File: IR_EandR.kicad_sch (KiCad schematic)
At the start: 4 parts, among them J4 IR Emitter, J6 Conn_01x04

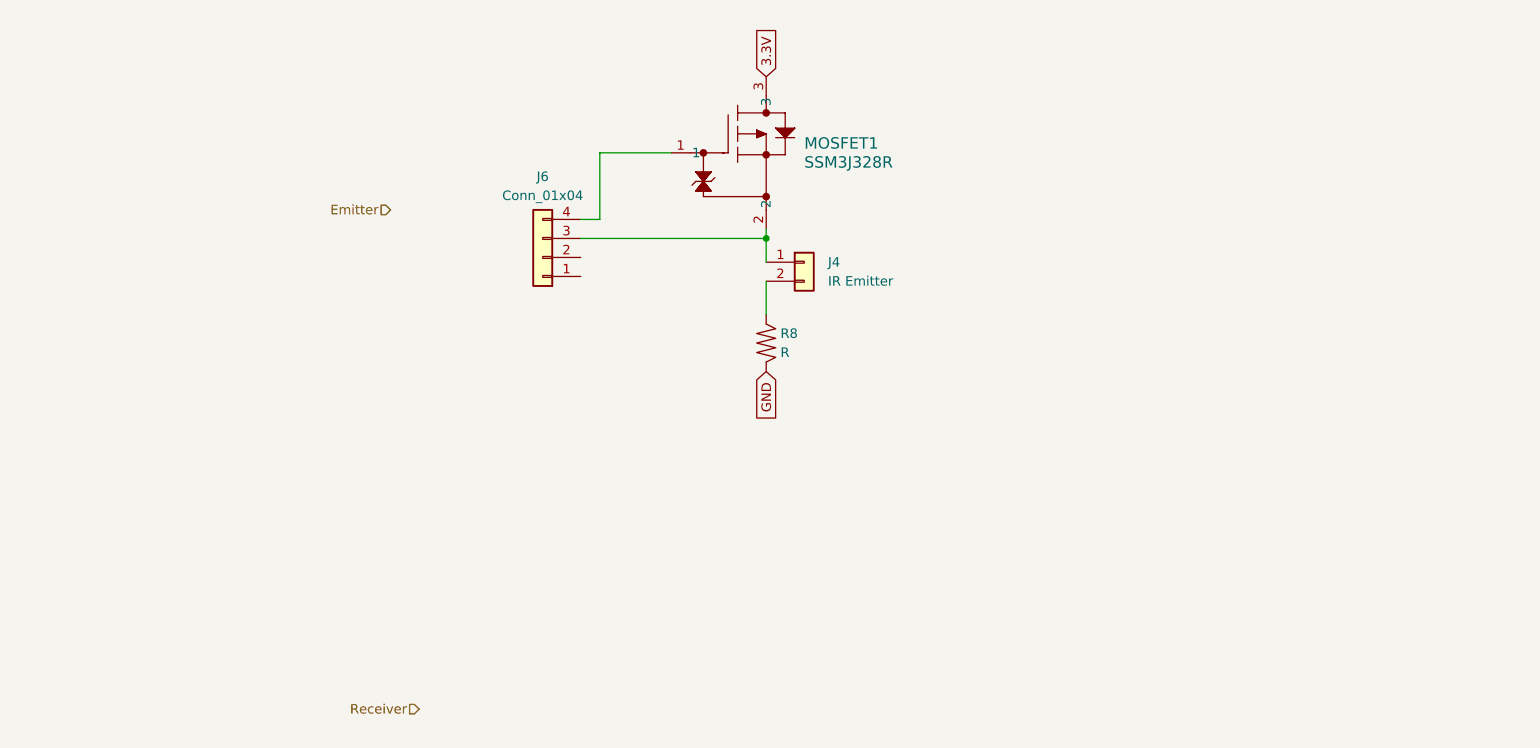
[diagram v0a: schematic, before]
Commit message: IR Receiver and Comparator
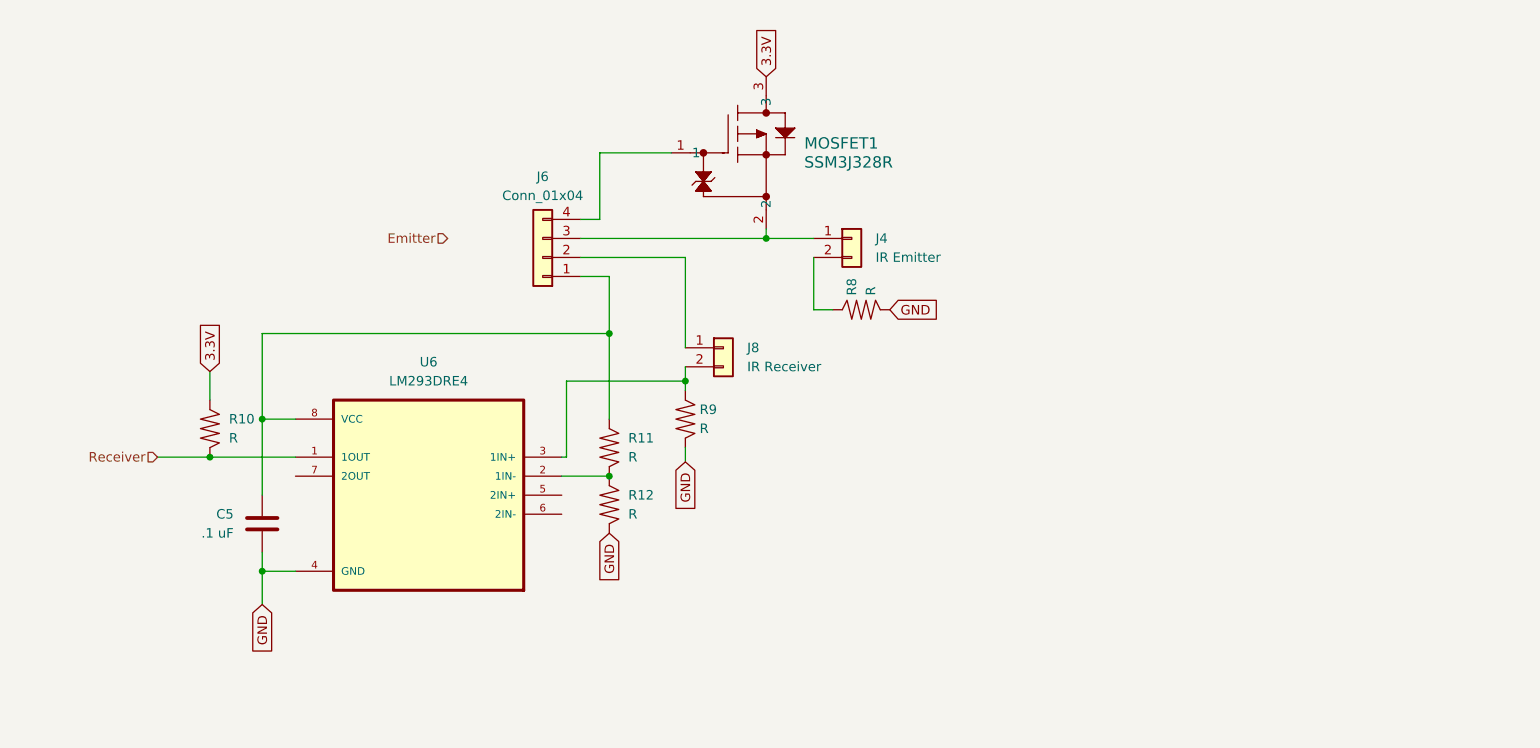
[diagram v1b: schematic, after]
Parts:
- added C5: .1 uF, symbol Hestres_Standard_Lib:C
- added J8: IR Receiver, symbol Connector_Generic:Conn_01x02
- added R10, R11, R12, R9: R, symbol Hestres_Standard_Lib:R
- added U6: LM293DRE4, LM293DRE4:SOIC127P599X175-8N, symbol ProjComparator:LM293DRE4
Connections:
- net 3.3V: now also R10.1
- net GND: now also C5.2, R12.2, R9.2, U6.4 (GND)
- net Receiver: now also R10.2, U6.1 (1OUT)
- net at J6.1 (Pin_1): now also C5.1, R11.1, U6.8 (VCC)
- net at J6.2 (Pin_2): now also J8.1 (Pin_1)
- new net: R11.2, R12.1, U6.2 (1IN-)
- new net: J8.2 (Pin_2), R9.1, U6.3 (1IN+)
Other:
- moved on the sheet: J4, R8

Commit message: Some cleanup
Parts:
- C5: footprint (none) -> Capacitor_SMD:C_0805_2012Metric
- MOSFET1: footprint SOT-23F_TOS -> (none)
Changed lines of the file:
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@@
       (effects (font (size 1.524 1.524)) (justify left))
     )
-    (property "Footprint" "SOT-23F_TOS" (at 130.175 49.53 0)
+    (property "Footprint" "" (at 130.175 49.53 0)
       (effects (font (size 1.27 1.27) italic) hide)
     )
@@
       (effects (font (size 1.27 1.27)) (justify left))
     )
-    (property "Footprint" "" (at 72.0598 110.49 0)
-      (effects (font (size 1.27 1.27)) hide)
-    )
+    (property "Footprint" "Capacitor_SMD:C_0805_2012Metric" (at 72.0598 110.49 0)
+      (effects (font (size 1.27 1.27)) hide)
+    )

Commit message: Remaining Footprints Assigned
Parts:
- J8: footprint (none) -> Connector_PinHeader_2.54mm:PinHeader_1x02_P2.54mm_Vertical
- MOSFET1: footprint (none) -> Proj:SOT-23F_TOS
- R10, R11, R12, R9: footprint (none) -> Resistor_SMD:R_0805_2012Metric
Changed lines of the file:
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@@
       (effects (font (size 1.524 1.524)) (justify left))
     )
-    (property "Footprint" "" (at 130.175 49.53 0)
+    (property "Footprint" "Proj:SOT-23F_TOS" (at 130.175 49.53 0)
       (effects (font (size 1.27 1.27) italic) hide)
     )
@@
       (effects (font (size 1.27 1.27)) (justify left))
     )
-    (property "Footprint" "" (at 117.602 96.52 90)
+    (property "Footprint" "Resistor_SMD:R_0805_2012Metric" (at 117.602 96.52 90)
       (effects (font (size 1.27 1.27)) hide)
     )
@@
       (effects (font (size 1.27 1.27)) (justify left))
     )
-    (property "Footprint" "" (at 127.762 92.71 90)
+    (property "Footprint" "Resistor_SMD:R_0805_2012Metric" (at 127.762 92.71 90)
       (effects (font (size 1.27 1.27)) hide)
     )
@@
       (effects (font (size 1.27 1.27)) (justify left))
     )
-    (property "Footprint" "" (at 64.262 93.98 90)
+    (property "Footprint" "Resistor_SMD:R_0805_2012Metric" (at 64.262 93.98 90)
       (effects (font (size 1.27 1.27)) hide)
     )
@@
       (effects (font (size 1.27 1.27)) (justify left))
     )
-    (property "Footprint" "" (at 117.602 104.14 90)
+    (property "Footprint" "Resistor_SMD:R_0805_2012Metric" (at 117.602 104.14 90)
       (effects (font (size 1.27 1.27)) hide)
     )
@@
       (effects (font (size 1.27 1.27)) (justify left))
     )
-    (property "Footprint" "" (at 134.62 83.185 0)
+    (property "Footprint" "Connector_PinHeader_2.54mm:PinHeader_1x02_P2.54mm_Vertical" (at 134.62 83.185 0)
       (effects (font (size 1.27 1.27)) hide)
     )

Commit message: Annotations
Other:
- note added: "Pins 1 and 2 of this jumper allow the comparator and IR Receiver to be driven at 3.3V or 18V."
- note added: "Pins 3 and 4 allow me to connect the IR Emitter directly to the MCU or through a FET to VCC. This will depend on how much current is needed for the distances I plan to send the IR beam. By using a through-pin IR Diode, I also leave myself open to switch to a laser emitter if needed."
- note added: "R11 and R12 control the voltage threshold for the comparator. Their values are left undefined on the test board until more testing can be done on the IR Receiver."
- note added: "The IR Emitter resistor will control the current pulled through the emitter. Its value is undefined on the test board"
- note added: "The IR Receiver is a phototransistor, which allows a certain current based on how many photons are striking it. R9 is set so that current creates a readable voltage. It is left undefined on the test board."
- moved on the sheet: C5, J8, R10, R11, R12, R9, U6

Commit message: Components on PCB, all warnings and error fixed
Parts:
- U6: footprint LM293DRE4:SOIC127P599X175-8N -> Proj:SOIC127P599X175-8N
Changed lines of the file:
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@@
       (effects (font (size 1.27 1.27)))
     )
-    (property "Footprint" "LM293DRE4:SOIC127P599X175-8N" (at 95.25 112.395 0)
+    (property "Footprint" "Proj:SOIC127P599X175-8N" (at 95.25 112.395 0)
       (effects (font (size 1.27 1.27)) (justify bottom) hide)
     )

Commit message: MCU Layout
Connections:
- net Vsup: now reaches C5.1, J6.1 (Pin_1), R11.1, U6.8 (VCC)
- net Emit_Direct: now reaches J4.1 (Pin_1), J6.3 (Pin_3), MOSFET1.2
- net Emit_MOS: now reaches J6.4 (Pin_4), MOSFET1.1
- net Vref: now reaches R11.2, R12.1, U6.2 (1IN-)
- net Vrec: now reaches J8.2 (Pin_2), R9.1, U6.3 (1IN+)
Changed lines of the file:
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@@
+    (effects (font (size 1.27 1.27)) (justify left bottom))
+  )
+  (label "Emit_MOS" (at 118.11 57.15 0) (fields_autoplaced)
+    (effects (font (size 1.27 1.27)) (justify left bottom))
+  )
+  (label "Rec_out" (at 69.215 107.315 0) (fields_autoplaced)
+    (effects (font (size 1.27 1.27)) (justify left bottom))
+  )
+  (label "Vref" (at 114.935 109.855 0) (fields_autoplaced)
+    (effects (font (size 1.27 1.27)) (justify left bottom))
+  )
+  (label "Emit_Direct" (at 122.555 68.58 0) (fields_autoplaced)
+    (effects (font (size 1.27 1.27)) (justify left bottom))
+  )
+  (label "Vsup" (at 106.68 90.805 0) (fields_autoplaced)
+    (effects (font (size 1.27 1.27)) (justify left bottom))
+  )
+  (label "Vrec" (at 114.3 97.155 0) (fields_autoplaced)
     (effects (font (size 1.27 1.27)) (justify left bottom))
   )

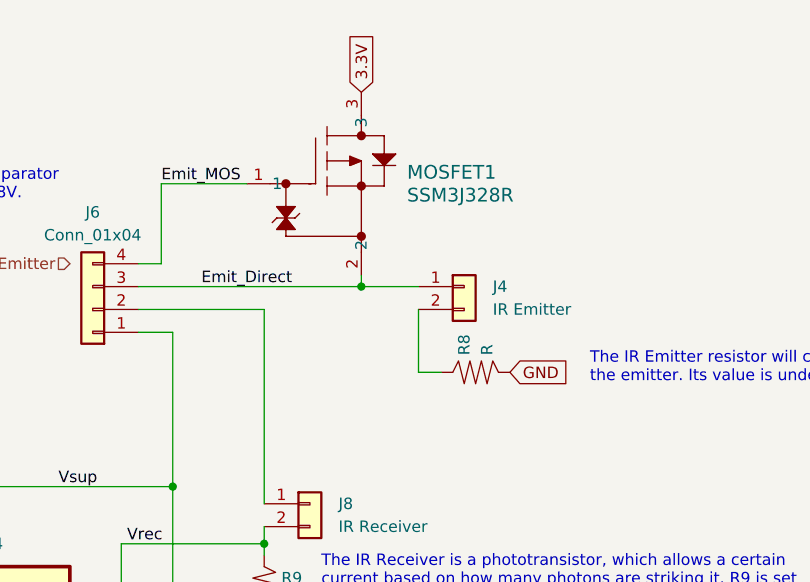
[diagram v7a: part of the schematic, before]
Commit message: Emitter, Receiver, and board outline
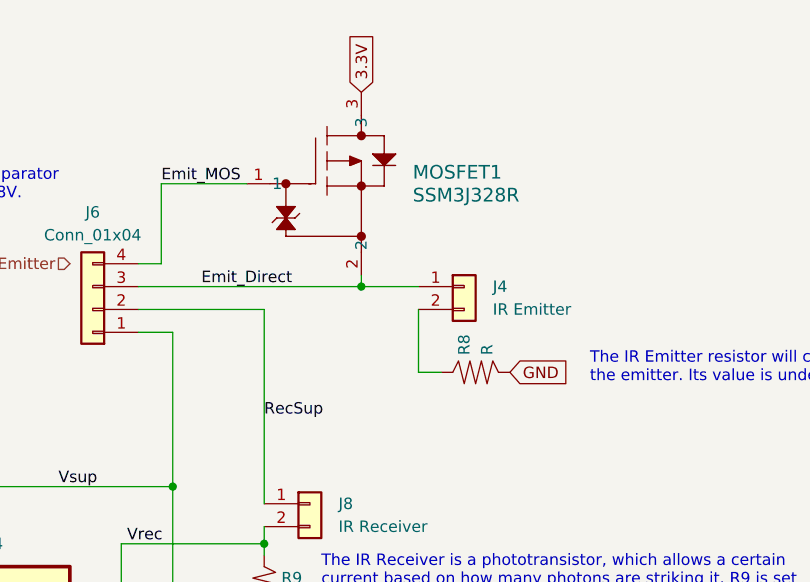
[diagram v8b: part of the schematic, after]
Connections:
- net RecSup: now reaches J6.2 (Pin_2), J8.1 (Pin_1)
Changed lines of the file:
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@@
+    (effects (font (size 1.27 1.27)) (justify left bottom))
+  )
+  (label "RecSup" (at 129.54 83.185 0) (fields_autoplaced)
     (effects (font (size 1.27 1.27)) (justify left bottom))
   )
@@
   (symbol (lib_id "ProjPMOS_LV:SSM3J328R") (at 130.175 49.53 0) (unit 1)
     (in_bom yes) (on_board yes) (dnp no) (fields_autoplaced)
-    (property "Reference" "MOSFET1" (at 145.415 55.88 0)
+    (property "Reference" "MOSFET1" (at 146.05 55.88 0)
       (effects (font (size 1.524 1.524)) (justify left))
     )
-    (property "Value" "SSM3J328R" (at 145.415 58.42 0)
+    (property "Value" "SSM3J328R" (at 146.05 58.42 0)
       (effects (font (size 1.524 1.524)) (justify left))
     )
@@
         )
         (path "/b94f5b10-ee0c-4425-b025-e3a8bb3cc7b0/e8cb00b1-5c92-44fb-a5f7-bb6e01e4cbd4"
-          (reference "MOSFET1") (unit 1)
+          (reference "FET1") (unit 1)
         )
       )
